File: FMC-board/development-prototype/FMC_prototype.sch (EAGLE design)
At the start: 55 parts, among them J1 DC_POWER_JACK-PJ-102AH, J2 DC_POWER_JACK-PJ-102AH

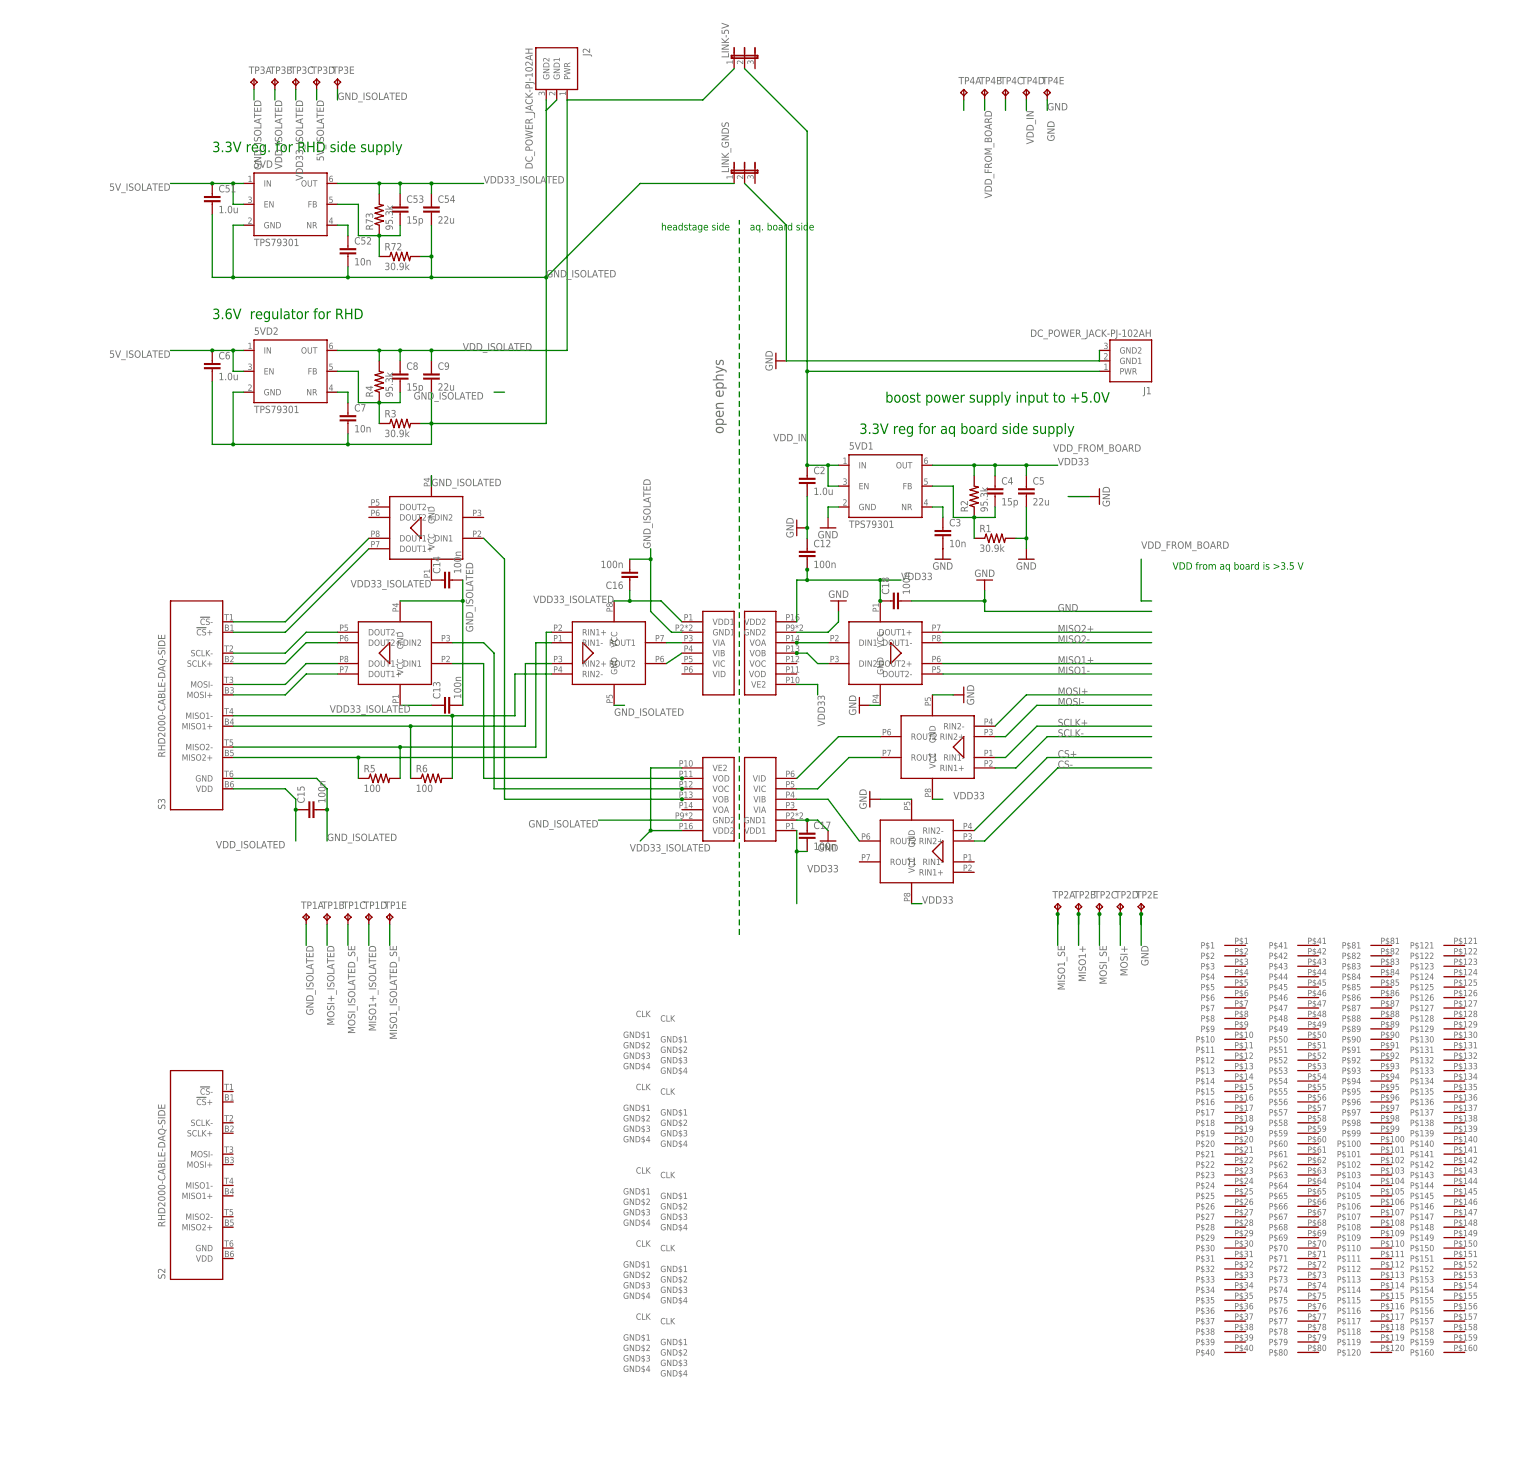
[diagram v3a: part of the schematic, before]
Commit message: more power layout
started adding pins on the LPC FMC connector
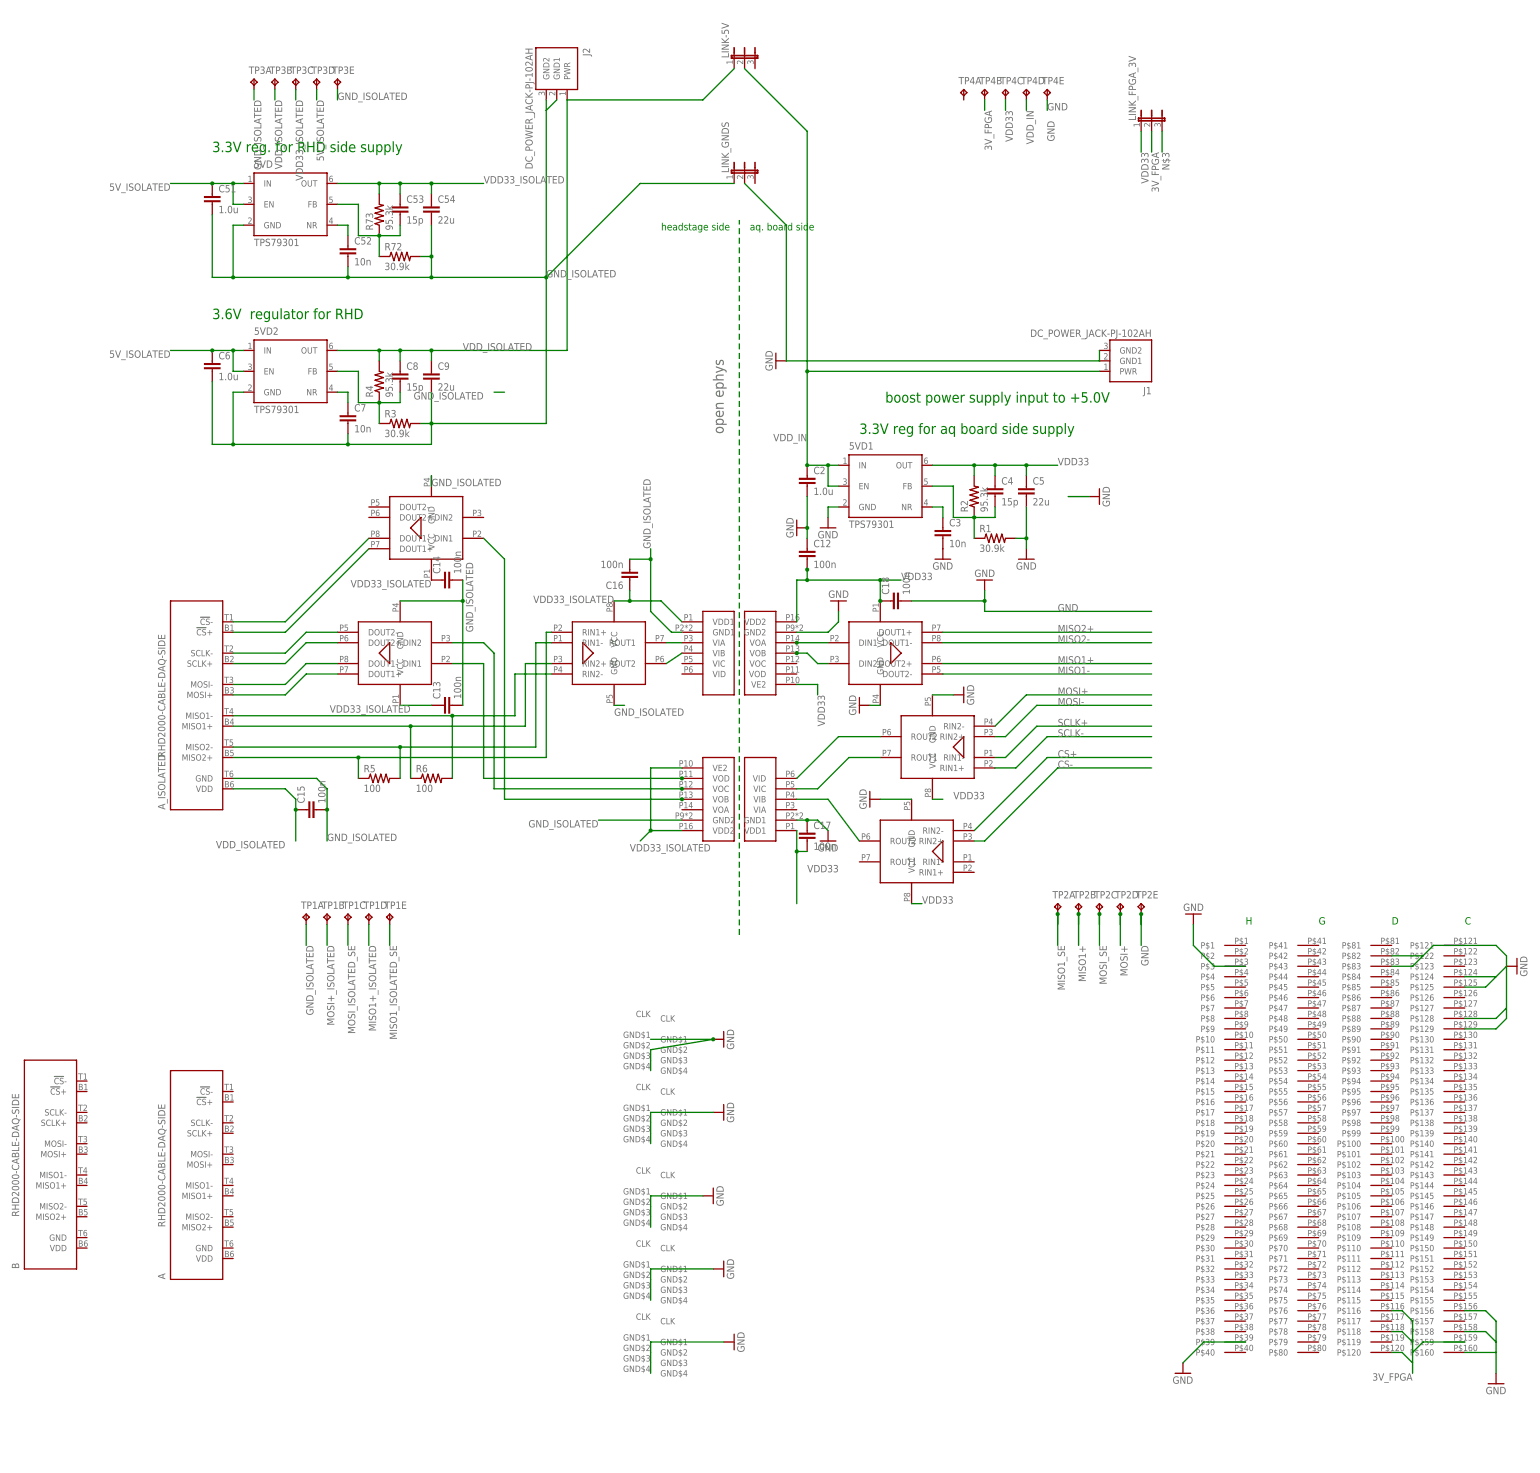
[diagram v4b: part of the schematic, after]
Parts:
- added B: RHD2000-CABLE-DAQ-SIDE, RHD2000_eval_board:RHD2000-CABLE-DAQ-SIDE
- added LINK_FPGA_3V: (no value), jumper:JP2E
- renumbered S2 to A, S3 to A_ISOLATED
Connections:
- removed net 5VBOOST: TP4A.TP
- removed net PWR_JACK: TP4C.TP
- removed net VDD_FROM_BOARD: TP4B.TP
- new net 3V_FPGA: LINK_FPGA_3V.2, TP4B.TP, U$4G$1.P$116, U$4G$1.P$118, U$4G$1.P$120, U$4G$1.P$159
- new net N$3: LINK_FPGA_3V.3
- net GND: now also U$13.GND$1, U$13.GND$2, U$13.GND$3, U$13.GND$4, U$14.GND$1, U$14.GND$2, U$14.GND$3, U$14.GND$4, U$15.GND$1, U$15.GND$2, U$15.GND$3, U$15.GND$4, U$2.GND$1, U$2.GND$2, U$2.GND$3, U$2.GND$4, U$4G$1.P$121, U$4G$1.P$124, U$4G$1.P$125, U$4G$1.P$128, U$4G$1.P$129, U$4G$1.P$156, U$4G$1.P$158, U$4G$1.P$160, U$4G$1.P$3, U$4G$1.P$39, U$4G$1.P$82, U$4G$1.P$83, U$5.GND$1, U$5.GND$2, U$5.GND$3, U$5.GND$4
- net VDD33: now also LINK_FPGA_3V.1, TP4C.TP
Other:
- note added: "C"
- note added: "D"
- note added: "G"
- note added: "H"
- note removed: "VDD from aq board is >3.5 V"

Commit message: added 3.6V regulator for non-isolated SPI connectors
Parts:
- added 5VD4: TPS79301, RHD2000_eval_board:TPS79301
- added C20: 1.0u, RHD2000_eval_board:C_0805
- added C21: 15p, RHD2000_eval_board:C_0603
- added C22: 22u, RHD2000_eval_board:C_1206
- added C23: 10n, RHD2000_eval_board:C_0603
- added R10: 30.9k, RHD2000_eval_board:R_0603
- added R9: 95.3k, RHD2000_eval_board:R_0603
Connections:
- new net N$10: A.MISO1+
- new net N$11: A.MISO2-
- new net N$12: A.MISO2+
- new net N$14: 5VD4.NR, C23.1
- new net N$17: B.MISO2+
- new net N$18: B.MISO2-
- new net N$19: B.MISO1+
- new net N$2: A.!CS!-
- new net N$20: B.MISO1-
- new net N$21: B.MOSI+
- new net N$22: B.MOSI-
- new net N$23: B.SCLK+
- new net N$24: B.SCLK-
- new net N$25: B.!CS!+
- new net N$26: B.!CS!-
- new net N$27: 5VD4.FB, C21.2, R10.1, R9.1
- new net N$4: A.!CS!+
- new net N$5: A.SCLK-
- new net N$6: A.SCLK+
- new net N$7: A.MOSI-
- new net N$8: A.MOSI+
- new net N$9: A.MISO1-
- new net VDD36: 5VD4.OUT, A.VDD, B.VDD, C21.1, C22.1, R9.2, TP4A.TP
- net GND: now also 5VD4.GND, A.GND, B.GND, C20.2, C22.2, C23.2, R10.2
- net VDD_IN: now also 5VD4.EN, 5VD4.IN, C20.1
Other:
- moved on the sheet: A, B

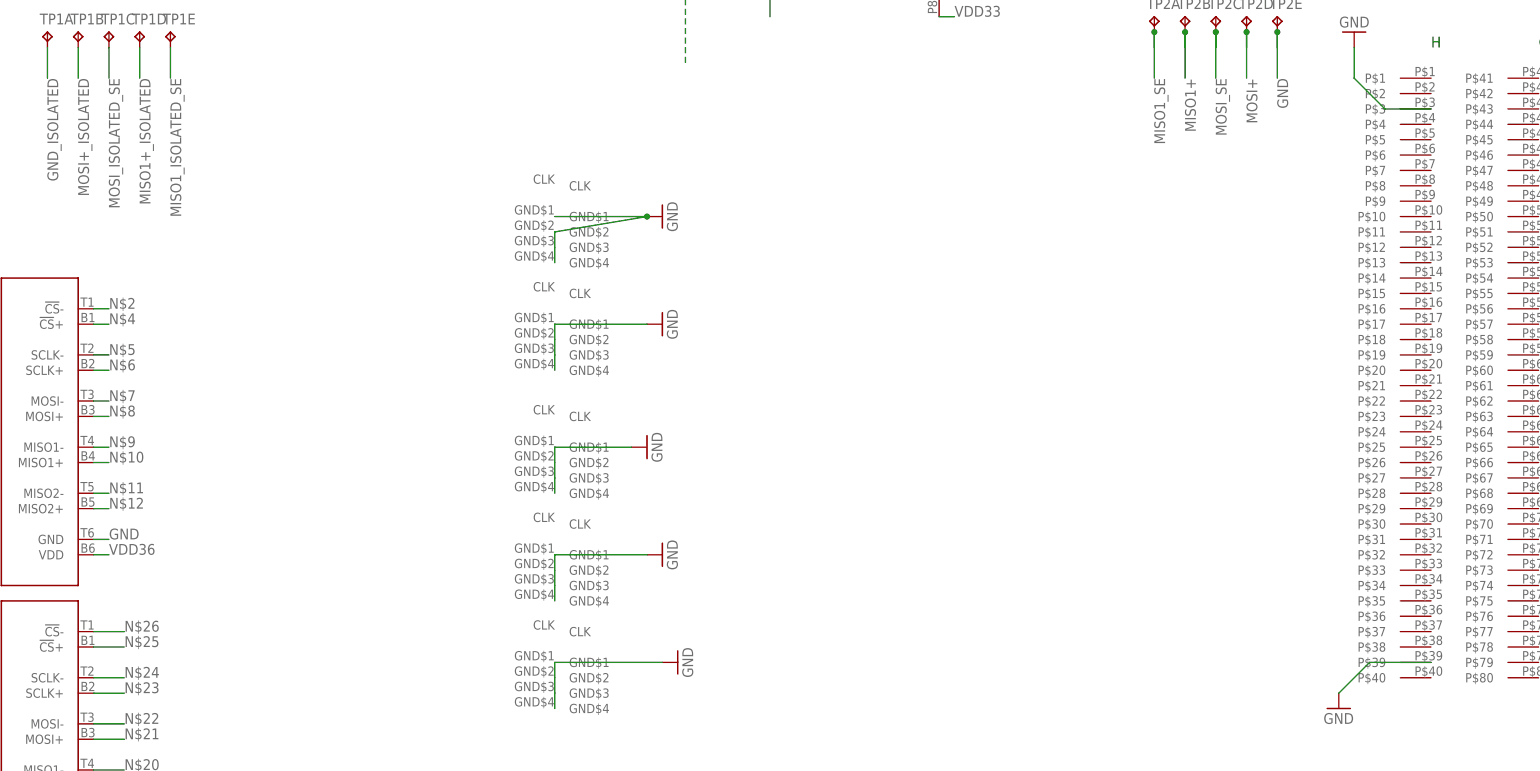
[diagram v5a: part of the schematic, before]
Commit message: started adding SPI signals for A
still not routed
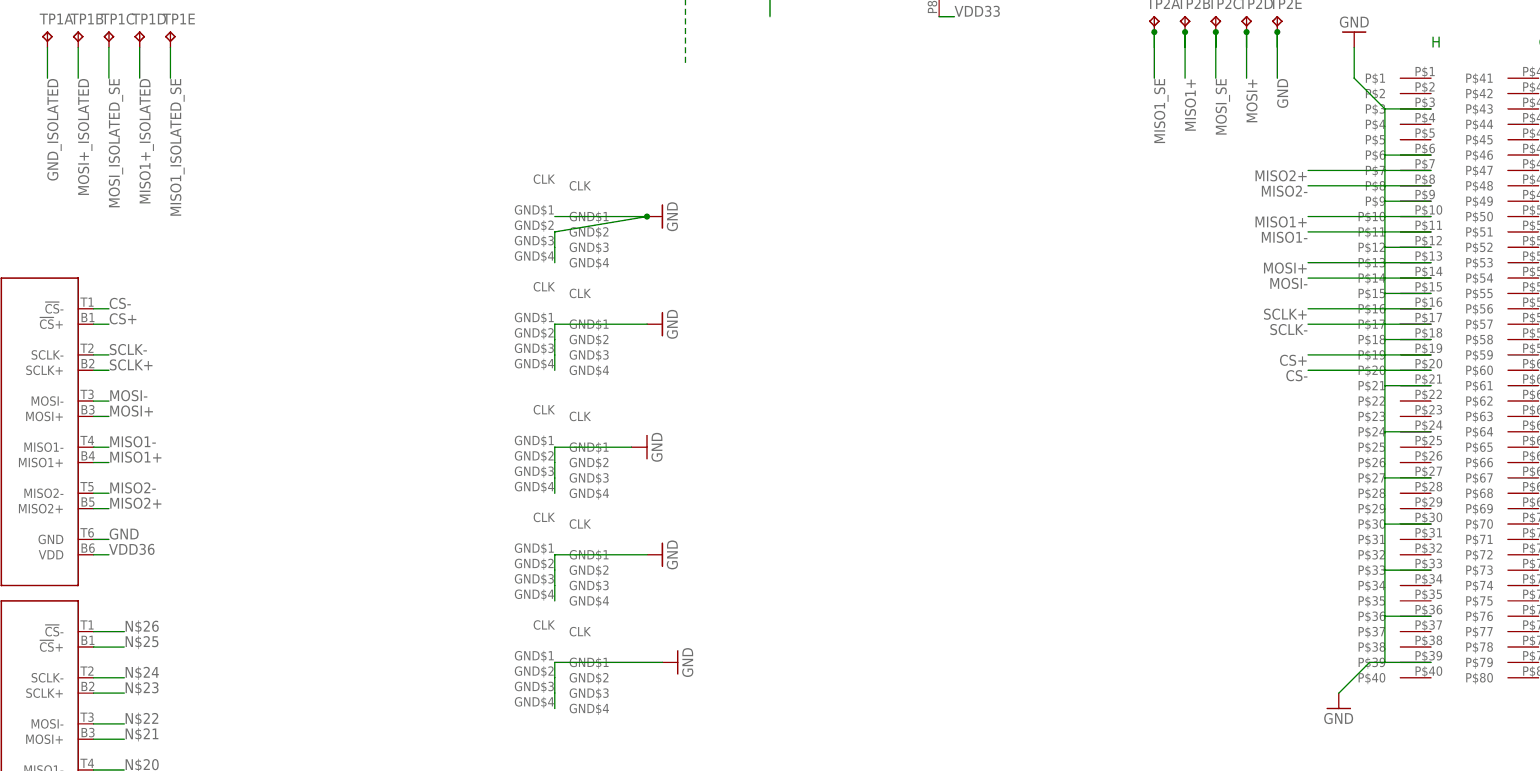
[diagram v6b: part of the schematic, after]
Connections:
- removed net N$10: A.MISO1+
- removed net N$11: A.MISO2-
- removed net N$12: A.MISO2+
- removed net N$2: A.!CS!-
- removed net N$4: A.!CS!+
- removed net N$5: A.SCLK-
- removed net N$6: A.SCLK+
- removed net N$7: A.MOSI-
- removed net N$8: A.MOSI+
- removed net N$9: A.MISO1-
- net CS+: now also A.!CS!+, U$4G$1.P$19
- net CS-: now also A.!CS!-, U$4G$1.P$20
- net GND: now also U$4G$1.P$12, U$4G$1.P$15, U$4G$1.P$18, U$4G$1.P$21, U$4G$1.P$24, U$4G$1.P$27, U$4G$1.P$30, U$4G$1.P$33, U$4G$1.P$36, U$4G$1.P$9
- net MISO1+: now also A.MISO1+, U$4G$1.P$10
- net MISO1-: now also A.MISO1-, U$4G$1.P$11
- net MISO2+: now also A.MISO2+, U$4G$1.P$7
- net MISO2-: now also A.MISO2-, U$4G$1.P$8
- net MOSI+: now also A.MOSI+, U$4G$1.P$13
- net MOSI-: now also A.MOSI-, U$4G$1.P$14
- net SCLK+: now also A.SCLK+, U$4G$1.P$16
- net SCLK-: now also A.SCLK-, U$4G$1.P$17
